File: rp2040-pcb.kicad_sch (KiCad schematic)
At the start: 38 parts

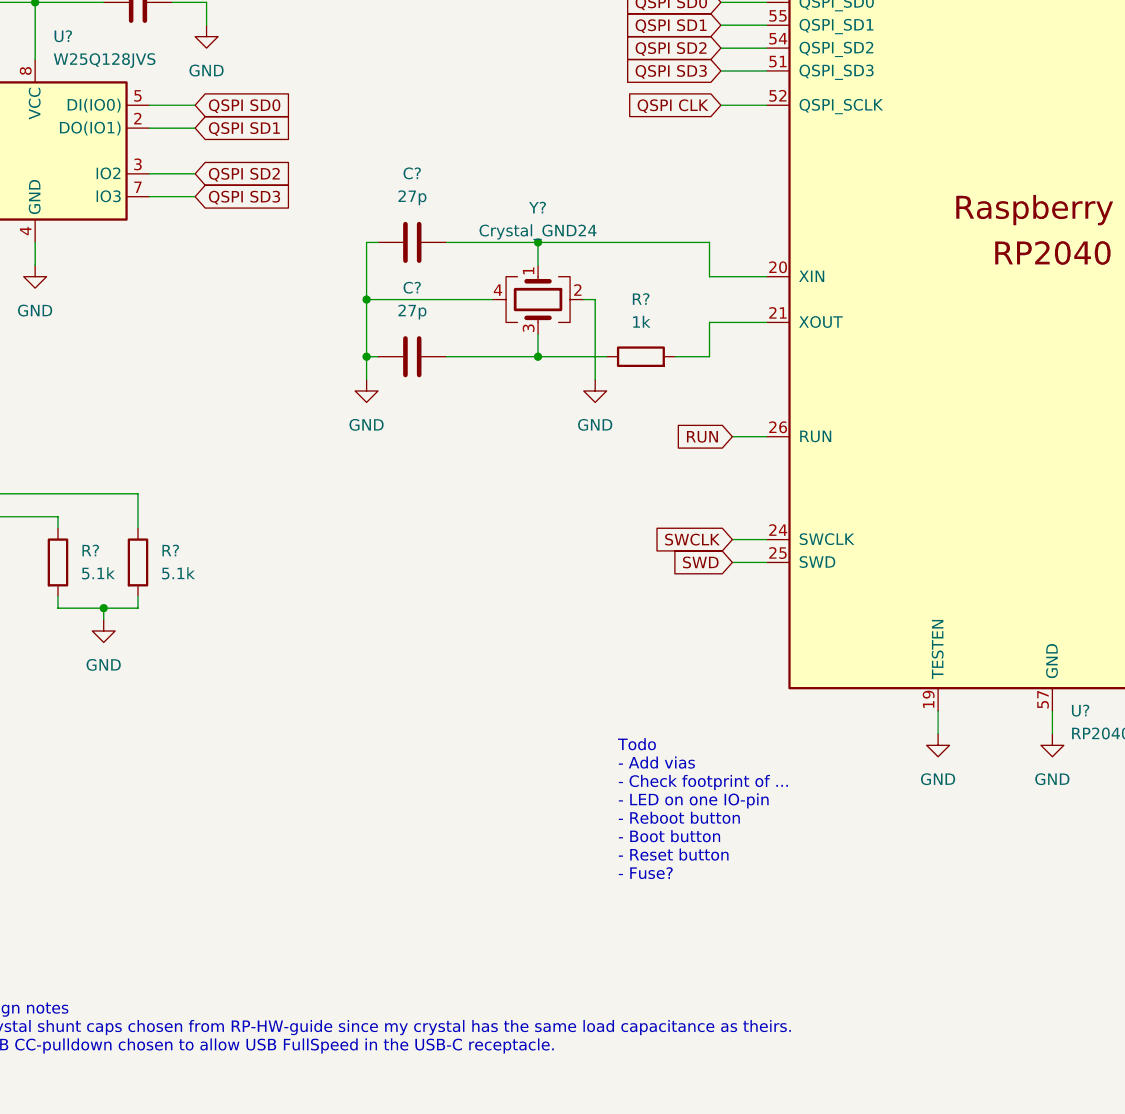
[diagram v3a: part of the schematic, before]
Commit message: Added reset-button.
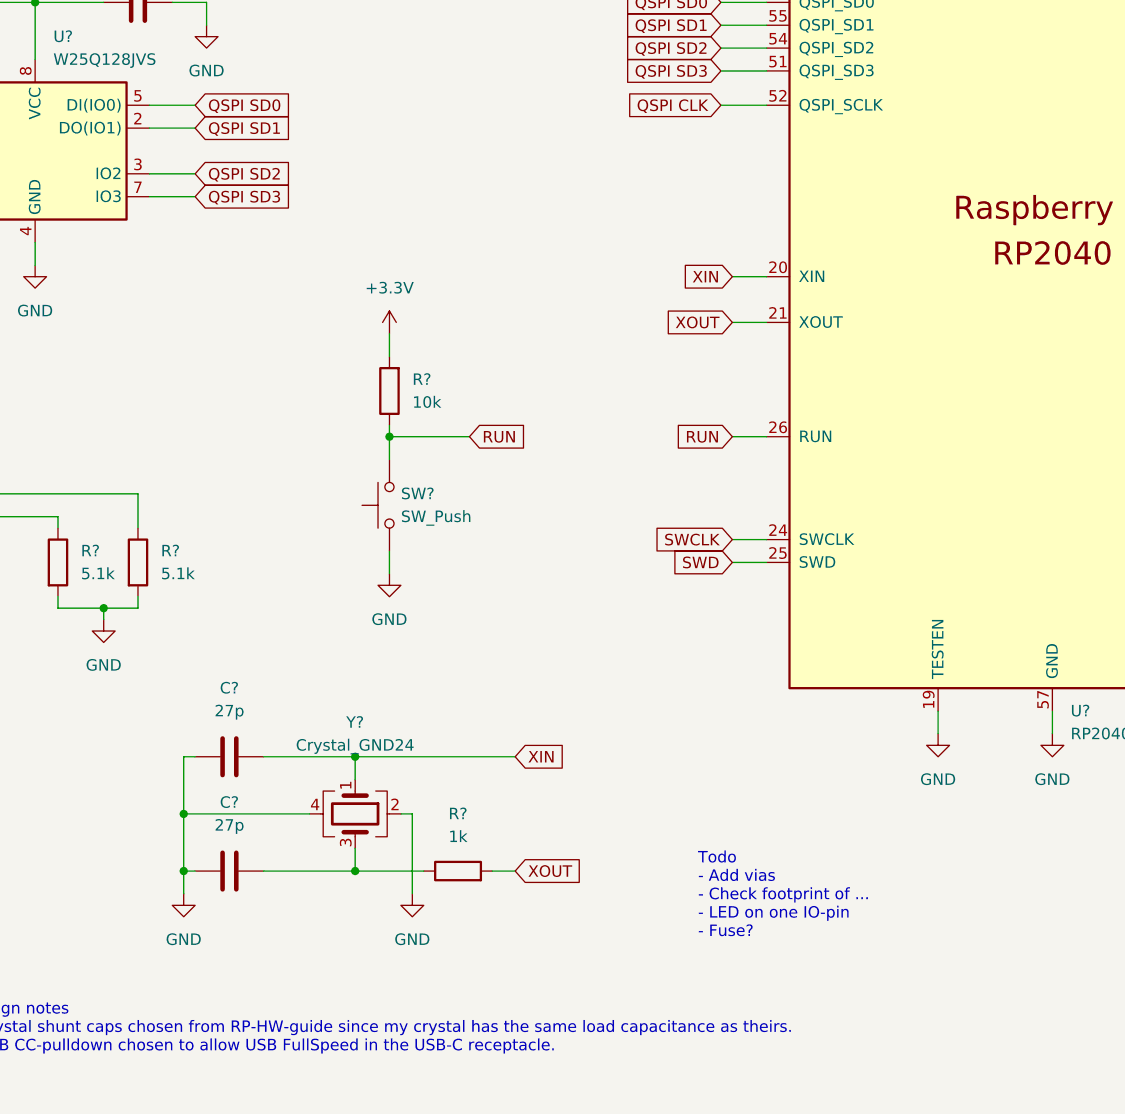
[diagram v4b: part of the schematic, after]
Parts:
- added R?: 10k, symbol Device:R
- added SW?: SW_Push, symbol Switch:SW_Push
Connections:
- net +3.3V: now also R?.2
- net GND: now also SW?.1
- net RUN: now also R?.1, SW?.2
- net XIN: now reaches C?.2, U?.20 (XIN), Y?.1
- net XOUT: now reaches R?.2, U?.21 (XOUT)
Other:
- note added: "Todo - Add vias - Check footprint of ... - LED on one IO-pin - Fuse?"
- note removed: "Todo - Add vias - Check footprint of ... - LED on one IO-pin - Reboot button - Boot button - Reset button - Fuse?"
- moved on the sheet: C?, R?, Y?

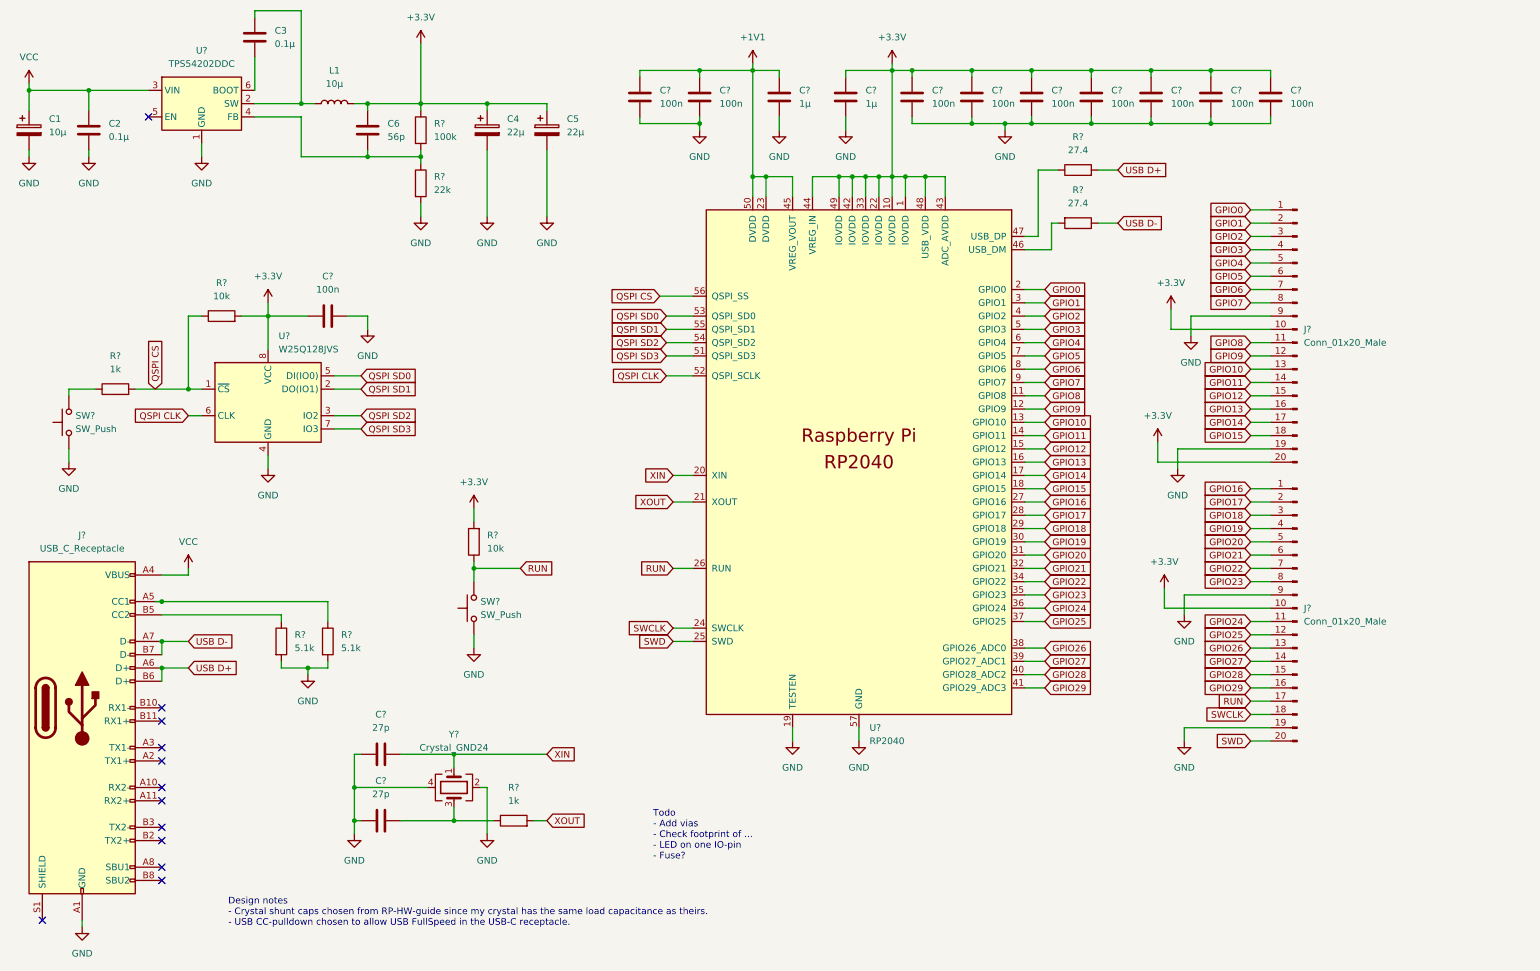
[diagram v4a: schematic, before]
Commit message: Added power LED.
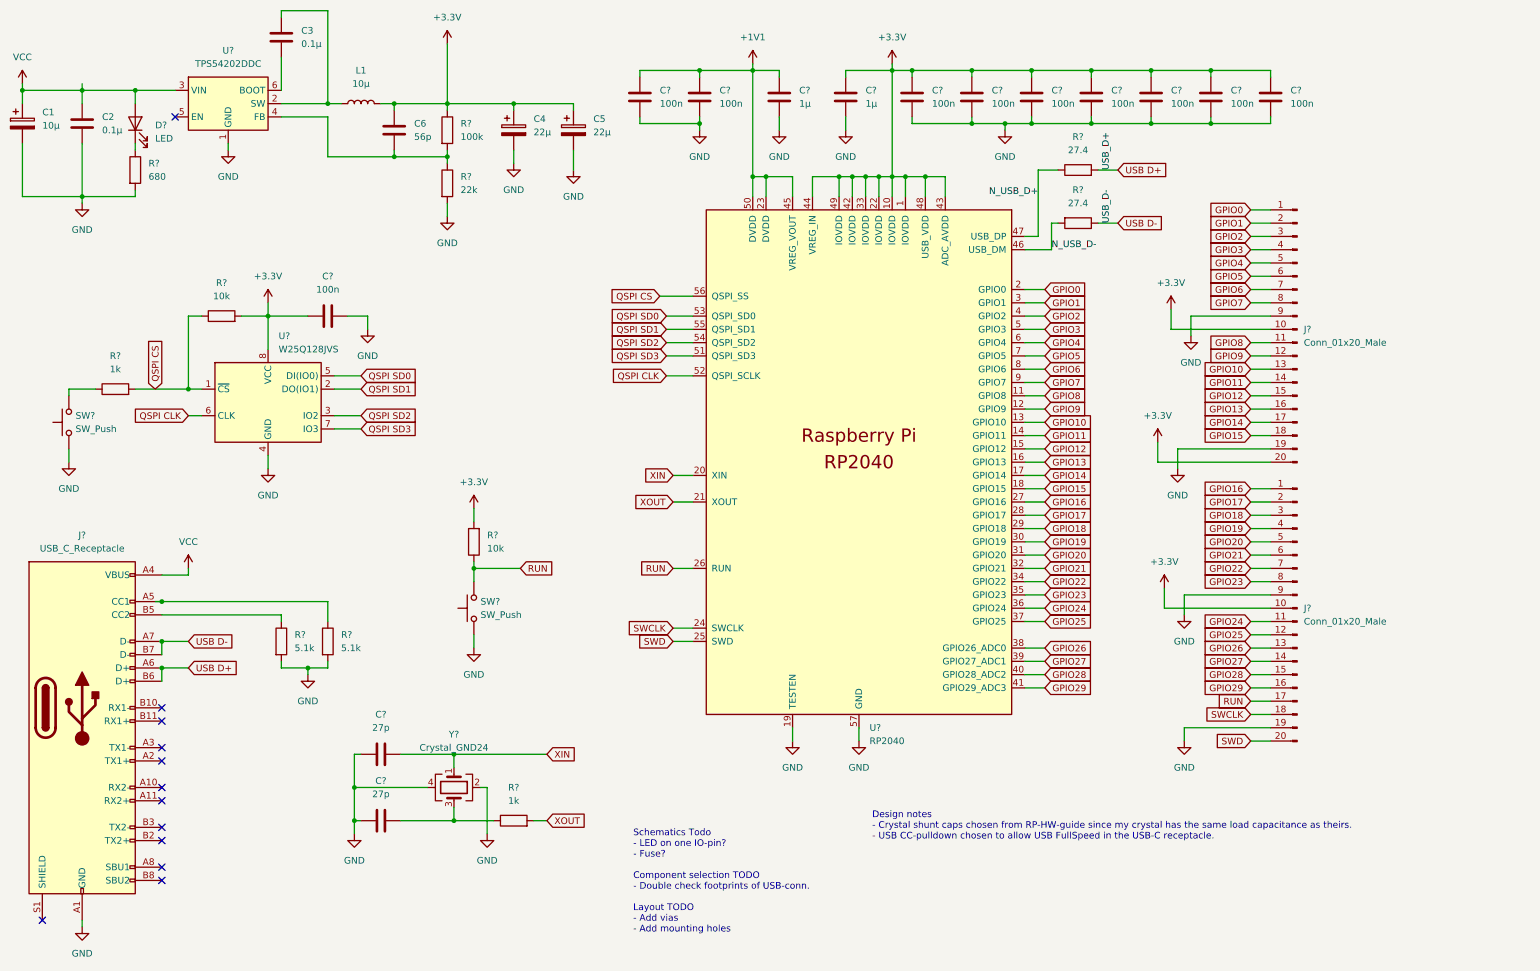
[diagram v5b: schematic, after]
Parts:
- added D?: LED, symbol Device:LED
- added R?: 680, symbol Device:R
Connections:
- net GND: now also R?.2
- net VCC: now also D?.2 (A)
- net N_USB_D+: now reaches R?.1, U?.47 (USB_DP)
- net N_USB_D-: now reaches R?.2, U?.46 (USB_DM)
- new net: D?.1 (K), R?.1
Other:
- note added: "Schematics Todo - LED on one IO-pin? - Fuse? Component selection TODO - Double check footprints of USB-conn. Layout TODO - Add vias - Add mounting holes"
- note removed: "Todo - Add vias - Check footprint of ... - LED on one IO-pin - Fuse?"
- moved on the sheet: C1, C2, C3, C4, C5, C6, L1, R?, U?

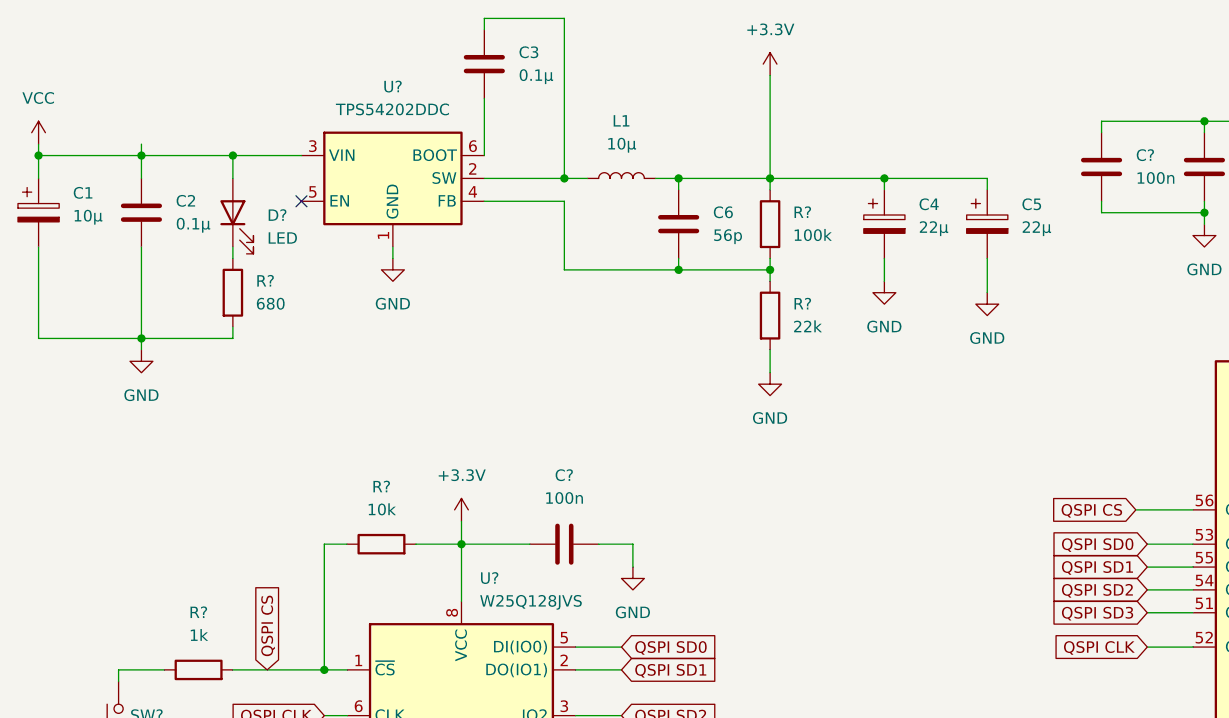
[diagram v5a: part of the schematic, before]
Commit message: Fixed missed resistor in voltage regulator.
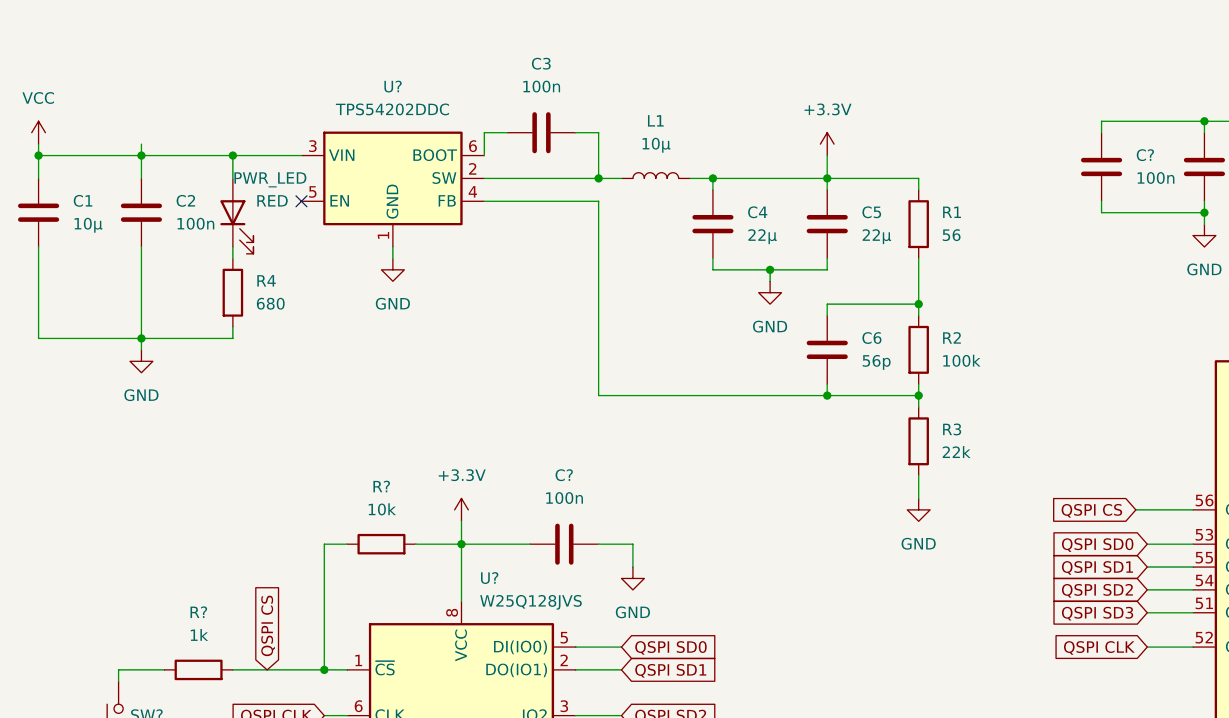
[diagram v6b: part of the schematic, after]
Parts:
- removed C1: 10µ, Capacitor_THT:CP_Radial_Tantal_D5.0mm_P2.50mm, symbol Device:C_Polarized
- removed C4, C5: 22µ, Capacitor_THT:CP_Radial_Tantal_D5.0mm_P2.50mm, symbol Device:C_Polarized
- added C1: 10µ, Capacitor_SMD:C_0805_2012Metric, symbol Device:C
- added C4, C5: 22µ, Capacitor_SMD:C_0805_2012Metric, symbol Device:C
- added R1: 56, symbol Device:R
- C2, C3: value 0.1µ -> 100n
- PWR_LED: renamed from D?; value LED -> RED
- gave numbers to parts that had none: 3
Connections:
- net +3.3V: now also C4.1, C5.1, R1.1; no longer C6.1, R2.1
- net GND: now also C1.2, C4.2, C5.2
- net VCC: now also C1.1
- net at L1.1, U?.2 (SW): now also C3.1; no longer C3.2
- net at U?.6 (BOOT): now also C3.2; no longer C3.1
- new net: C6.1, R1.2, R2.1
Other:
- moved on the sheet: C3, C6, L1, R2, R3

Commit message: Added annotations.
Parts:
- gave numbers to parts that had none: 31
- renumbered PWR_LED to PWR_LED1
